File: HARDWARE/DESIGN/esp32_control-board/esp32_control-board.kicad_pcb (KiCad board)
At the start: 2 copper layers, 130 x 105 mm, 140 parts, among them J1 Lock1, J10 ESP32-Prog, J11 RFID-module1, J12 RFID-module2, J15 Lamp1, J16 Lamp2, J17 Lamp3, J18 Lamp4, J19 Lamp5, J2 Lock2, J20 Lamp6, J21 Lamp7, J22 Lamp8, J3 Lock3, J301 ESP32m_Prog, J4 Lock4, J5 Lock5, J6 Lock6, J7 Lock7, J8 Lock8, J9 Power-in, Q1 AO4407C, SW301 Reset, SW302 Boot, U1 ESP32-S3-WROOM-1, U10 PC817, U11 PC817, U12 PC817, U13 PC817, U14 PC817, U15 PC817, U16 PC817, U2 LM63615DQDRRRQ1, U302 USBLC6-2SC6, U4 AMS1117-3.3, U5 PC817, U6 TBD62783A, U7 MCP23008-xSS, U8 MCP23008-xSS, U9 TBD62783A

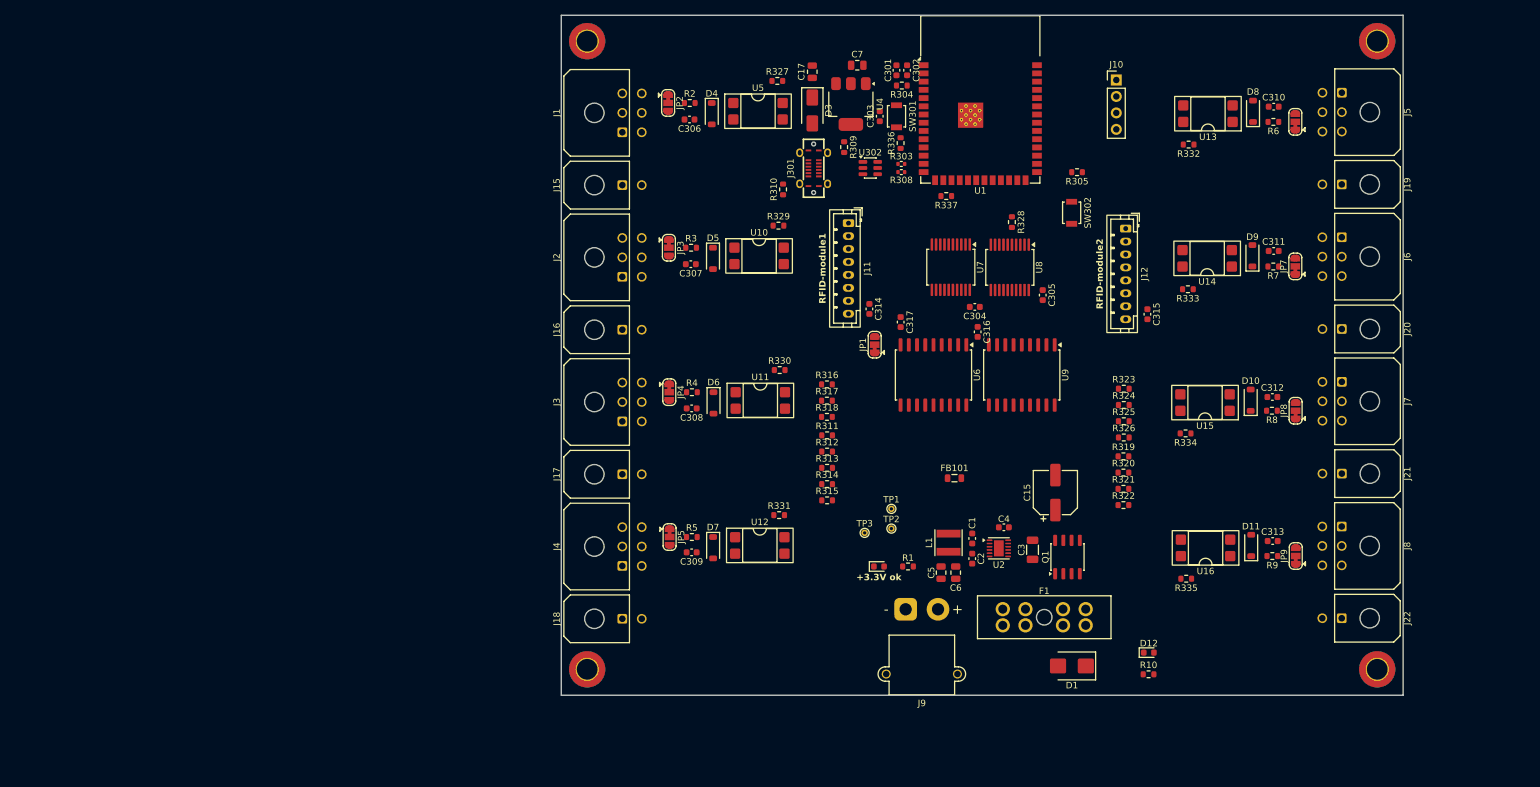
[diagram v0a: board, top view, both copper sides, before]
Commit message: 60710 - schematic and PCB-layout updated
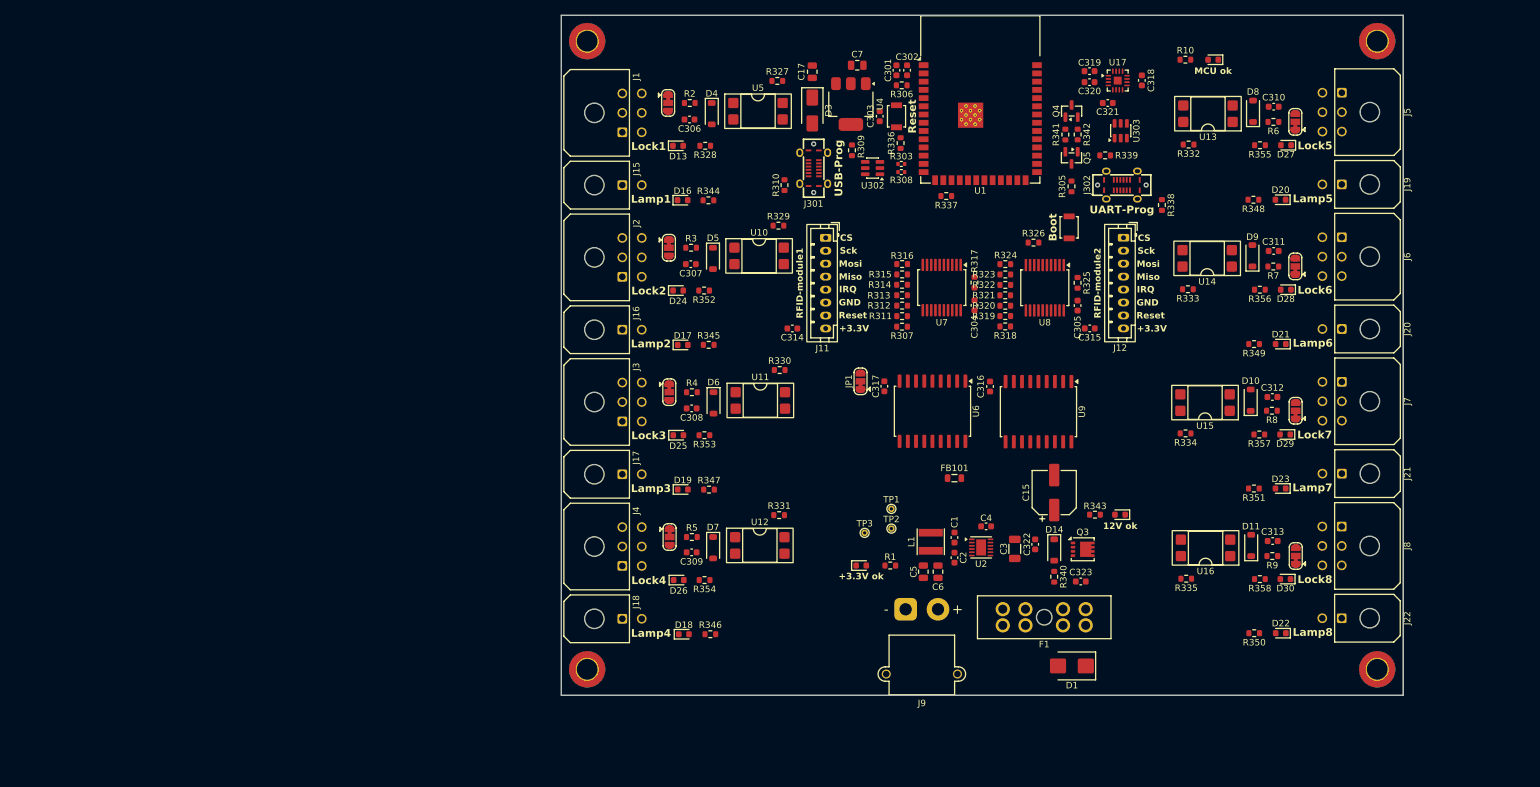
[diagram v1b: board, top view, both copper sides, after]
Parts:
- removed J10: ESP32-Prog, Connector_PinHeader_2.54mm:PinHeader_1x04_P2.54mm_Vertical
- removed Q1: AO4407C, (FOOTPRINTS):SOIC-8_P-MOSFET
- removed R304: 10k, Resistor_SMD:R_0603_1608Metric
- added C318: 100n, Capacitor_SMD:C_0603_1608Metric, F.Cu at (159.9, 60.0)
- added C319: 100n, Capacitor_SMD:C_0603_1608Metric, F.Cu at (151.8, 58.5)
- added C320: 100n, Capacitor_SMD:C_0603_1608Metric, F.Cu at (151.8, 60.2)
- added C321: 100n, Capacitor_SMD:C_0603_1608Metric, F.Cu at (154.6, 63.5)
- added C322: 100n, Capacitor_SMD:C_0603_1608Metric, F.Cu at (143.4, 131.6)
- added C323: 100n, Capacitor_SMD:C_0603_1608Metric, F.Cu at (150.5, 137.3)
- added D13: LOCK on, LED_SMD:LED_0603_1608Metric, F.Cu at (88.3, 70.1)
- added D14: MMSZ5242B, Diode_SMD:D_SOD-123, F.Cu at (146.4, 132.5)
- added D15: MCU ok, LED_SMD:LED_0603_1608Metric, F.Cu at (170.9, 56.8)
- added D16: LAMP on, LED_SMD:LED_0603_1608Metric, F.Cu at (89.0, 78.5)
- added D17: LAMP on, LED_SMD:LED_0603_1608Metric, F.Cu at (89.0, 100.8)
- added D18: LAMP on, LED_SMD:LED_0603_1608Metric, F.Cu at (89.2, 145.5)
- added D19: LAMP on, LED_SMD:LED_0603_1608Metric, F.Cu at (89.0, 123.1)
- added D20: LAMP on, LED_SMD:LED_0603_1608Metric, F.Cu at (181.3, 78.4)
- added D21: LAMP on, LED_SMD:LED_0603_1608Metric, F.Cu at (181.3, 100.7)
- added D22: LAMP on, LED_SMD:LED_0603_1608Metric, F.Cu at (181.4, 145.3)
- added D23: LAMP on, LED_SMD:LED_0603_1608Metric, F.Cu at (181.3, 123.0)
- added D24: LOCK on, LED_SMD:LED_0603_1608Metric, F.Cu at (88.3, 92.4)
- added D25: LOCK on, LED_SMD:LED_0603_1608Metric, F.Cu at (88.3, 114.8)
- added D26: LOCK on, LED_SMD:LED_0603_1608Metric, F.Cu at (88.4, 137.1)
- added D27: LOCK on, LED_SMD:LED_0603_1608Metric, F.Cu at (182.2, 70.0)
- added D28: LOCK on, LED_SMD:LED_0603_1608Metric, F.Cu at (182.1, 92.3)
- added D29: LOCK on, LED_SMD:LED_0603_1608Metric, F.Cu at (182.0, 114.7)
- added D30: LOCK on, LED_SMD:LED_0603_1608Metric, F.Cu at (182.1, 137.0)
- added J302: UART-Prog, (FOOTPRINTS):C3151749_USB_TYPE-C_Vertical, F.Cu at (156.8, 76.1)
- added Q3: DMP3013SFV-7, Package_SON:Diodes_PowerDI3333-8, F.Cu at (150.8, 132.4)
- added Q4: SS8050, Package_TO_SOT_SMD:SOT-23, F.Cu at (149.1, 64.7)
- added Q5: SS8050, Package_TO_SOT_SMD:SOT-23, F.Cu at (149.0, 71.9)
- added R306: 12k, Resistor_SMD:R_0603_1608Metric, F.Cu at (122.8, 60.7)
- added R307: 12k, Resistor_SMD:R_0603_1608Metric, F.Cu at (122.9, 98.0)
- added R338: 5k1, Resistor_SMD:R_0603_1608Metric, F.Cu at (163.0, 79.2)
- added R339: 5k1, Resistor_SMD:R_0603_1608Metric, F.Cu at (154.2, 71.5)
- added R340: 12k, Resistor_SMD:R_0603_1608Metric, F.Cu at (146.4, 136.6)
- added R341: 12k, Resistor_SMD:R_0603_1608Metric, F.Cu at (148.1, 68.3)
- added R342: 12k, Resistor_SMD:R_0603_1608Metric, F.Cu at (150.0, 68.3)
- added R343: 5k1, Resistor_SMD:R_0603_1608Metric, F.Cu at (152.7, 127.0)
- added R344: 5k1, Resistor_SMD:R_0603_1608Metric, F.Cu at (93.0, 78.5)
- added R345: 5k1, Resistor_SMD:R_0603_1608Metric, F.Cu at (93.0, 100.8)
- added R346: 5k1, Resistor_SMD:R_0603_1608Metric, F.Cu at (93.3, 145.5)
- added R347: 5k1, Resistor_SMD:R_0603_1608Metric, F.Cu at (93.1, 123.2)
- added R348: 5k1, Resistor_SMD:R_0603_1608Metric, F.Cu at (177.1, 78.4)
- added R349: 5k1, Resistor_SMD:R_0603_1608Metric, F.Cu at (177.2, 100.7)
- added R350: 5k1, Resistor_SMD:R_0603_1608Metric, F.Cu at (177.3, 145.3)
- added R351: 5k1, Resistor_SMD:R_0603_1608Metric, F.Cu at (177.2, 123.0)
- added R352: 5k1, Resistor_SMD:R_0603_1608Metric, F.Cu at (92.3, 92.4)
- added R353: 5k1, Resistor_SMD:R_0603_1608Metric, F.Cu at (92.4, 114.8)
- added R354: 5k1, Resistor_SMD:R_0603_1608Metric, F.Cu at (92.4, 137.1)
- added R355: 5k1, Resistor_SMD:R_0603_1608Metric, F.Cu at (178.1, 70.0)
- added R356: 5k1, Resistor_SMD:R_0603_1608Metric, F.Cu at (178.1, 92.3)
- added R357: 5k1, Resistor_SMD:R_0603_1608Metric, F.Cu at (178.0, 114.7)
- added R358: 5k1, Resistor_SMD:R_0603_1608Metric, F.Cu at (178.1, 137.0)
- added U17: CH343P, Package_DFN_QFN:TQFN-16-1EP_3x3mm_P0.5mm_EP1.23x1.23mm, F.Cu at (156.2, 60.0)
- added U303: USBLC6-2SC6, Package_TO_SOT_SMD:SOT-23-6, F.Cu at (156.6, 67.8)
- J301: value ESP32m_Prog -> USB-Prog
- R305, R311, R312, R313, R314, R315, R316, R317, R318, R319, R320, R321, R322, R323, R324, R325, R326: value 10k -> 12k
- R328: value 10k -> 5k1
- moved R10 95.1 mm to (166.6, 56.8)
- moved R328 48.8 mm to (92.5, 70.1), turned to 0 degrees
- moved R322 38.6 mm to (138.8, 91.5), turned to 180 degrees
- moved R315 36.8 mm to (122.9, 89.9), turned to 180 degrees
- moved R321 35.0 mm to (138.8, 93.2), turned to 180 degrees
- moved R326 33.2 mm to (143.2, 85.0)
- moved R314 32.9 mm to (122.9, 91.5), turned to 180 degrees
- moved R320 31.6 mm to (138.8, 94.8), turned to 180 degrees
- moved R318 30.9 mm to (138.8, 98.0), turned to 180 degrees
- moved R317 29.2 mm to (134.1, 91.2), turned to -90 degrees
- moved R313 29.1 mm to (122.9, 93.1), turned to 180 degrees
- moved R324 28.4 mm to (138.8, 88.3), turned to 180 degrees
- moved R319 28.3 mm to (138.8, 96.4), turned to 180 degrees
- moved R323 25.4 mm to (138.8, 89.9), turned to 180 degrees
- moved R312 25.3 mm to (122.9, 94.8), turned to 180 degrees
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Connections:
- C317 pad 1: GND -> Net-(JP1-C)
- C317 pad 2: Net-(JP1-C) -> GND
- J301 pad A6: espM_USB_dp -> espU_USB_dp
- J301 pad A7: espM_USB_dm -> espU_USB_dm
- J301 pad B6: espM_USB_dp -> espU_USB_dp
- J301 pad B7: espM_USB_dm -> espU_USB_dm
- R10 pad 1: SWITCH1-COM -> esp_LED
- R10 pad 2: Net-(D12-A) -> Net-(D15-A)
- R303 pad 1: espM_USB_d- -> espU_USB_d-
- R308 pad 1: espM_USB_d+ -> espU_USB_d+
- R311 pad 1: Net-(U6-I1) -> Net-(U6-I7)
- R312 pad 1: Net-(U6-I2) -> Net-(U6-I6)
- R313 pad 1: Net-(U6-I3) -> Net-(U6-I5)
- R315 pad 1: Net-(U6-I5) -> Net-(U6-I3)
- R316 pad 1: Net-(U6-I6) -> Net-(U6-I2)
- R317 pad 1: Net-(U6-I7) -> Net-(U6-I1)
- R318 pad 1: Net-(U6-I8) -> Net-(U8-GP0)
- R319 pad 1: Net-(U8-GP0) -> Net-(U8-GP1)
- R320 pad 1: Net-(U8-GP1) -> Net-(U8-GP2)
- R321 pad 1: Net-(U8-GP2) -> Net-(U8-GP3)
- R322 pad 1: Net-(U8-GP3) -> Net-(U8-GP4)
- R323 pad 1: Net-(U8-GP4) -> Net-(U8-GP5)
- R324 pad 1: Net-(U8-GP5) -> Net-(U8-GP6)
- R325 pad 1: Net-(U8-GP6) -> Net-(U8-GP7)
- R326 pad 1: Net-(U8-GP7) -> +3V3
- R326 pad 2: GND -> Net-(U8-A0)
- R328 pad 1: +3V3 -> Net-(D13-A)
- R328 pad 2: Net-(U8-A0) -> LOCK1_ctrl
- U1 pad 36: esp_Rx -> esp_RXD
- U1 pad 37: esp_Tx -> esp_TXD
- U1 pad 39: unconnected-(U1-IO1-Pad39) -> esp_LED
- U302 pad 1: espM_USB_dm -> espU_USB_d+
- U302 pad 3: espM_USB_dp -> espU_USB_d-
- U302 pad 4: espM_USB_d+ -> espU_USB_dm
- U302 pad 6: espM_USB_d- -> espU_USB_dp
- U6 pad 11: LOCK8_ctrl -> LOCK1_ctrl
- U6 pad 12: LOCK7_ctrl -> LOCK2_ctrl
- U6 pad 13: LOCK6_ctrl -> LOCK3_ctrl
- U6 pad 14: LOCK5_ctrl -> LOCK4_ctrl
- U6 pad 15: LOCK4_ctrl -> LOCK5_ctrl
- U6 pad 16: LOCK3_ctrl -> LOCK6_ctrl
- U6 pad 17: LOCK2_ctrl -> LOCK7_ctrl
- U6 pad 18: LOCK1_ctrl -> LOCK8_ctrl
- U7 pad 12: Net-(U6-I1) -> Net-(U6-I8)
- U7 pad 13: Net-(U6-I2) -> Net-(U6-I7)
- U7 pad 14: Net-(U6-I3) -> Net-(U6-I6)
- U7 pad 15: Net-(U6-I4) -> Net-(U6-I5)
- U7 pad 16: Net-(U6-I5) -> Net-(U6-I4)
- U7 pad 17: Net-(U6-I6) -> Net-(U6-I3)
- U7 pad 18: Net-(U6-I7) -> Net-(U6-I2)
- U7 pad 19: Net-(U6-I8) -> Net-(U6-I1)
- U9 pad 1: Net-(U8-GP0) -> Net-(U8-GP7)
- U9 pad 11: LAMP8 -> LAMP1
- U9 pad 12: LAMP7 -> LAMP2
- U9 pad 13: LAMP6 -> LAMP3
- U9 pad 14: LAMP5 -> LAMP4
- U9 pad 15: LAMP4 -> LAMP5
- U9 pad 16: LAMP3 -> LAMP6
- U9 pad 17: LAMP2 -> LAMP7
- U9 pad 18: LAMP1 -> LAMP8
- U9 pad 2: Net-(U8-GP1) -> Net-(U8-GP6)
- U9 pad 3: Net-(U8-GP2) -> Net-(U8-GP5)
- U9 pad 4: Net-(U8-GP3) -> Net-(U8-GP4)
- U9 pad 5: Net-(U8-GP4) -> Net-(U8-GP3)
- U9 pad 6: Net-(U8-GP5) -> Net-(U8-GP2)
- U9 pad 7: Net-(U8-GP6) -> Net-(U8-GP1)
- U9 pad 8: Net-(U8-GP7) -> Net-(U8-GP0)
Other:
- board text added: "+3.3V"
- board text added: "CS"
- board text added: "GND"
- board text added: "IRQ"
- board text added: "Miso"
- board text added: "Mosi"
- board text added: "Reset"
- board text added: "Sck"

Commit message: 60714 - one of two I2C-mux ICs was removed, PCB-layout finished, start tracing
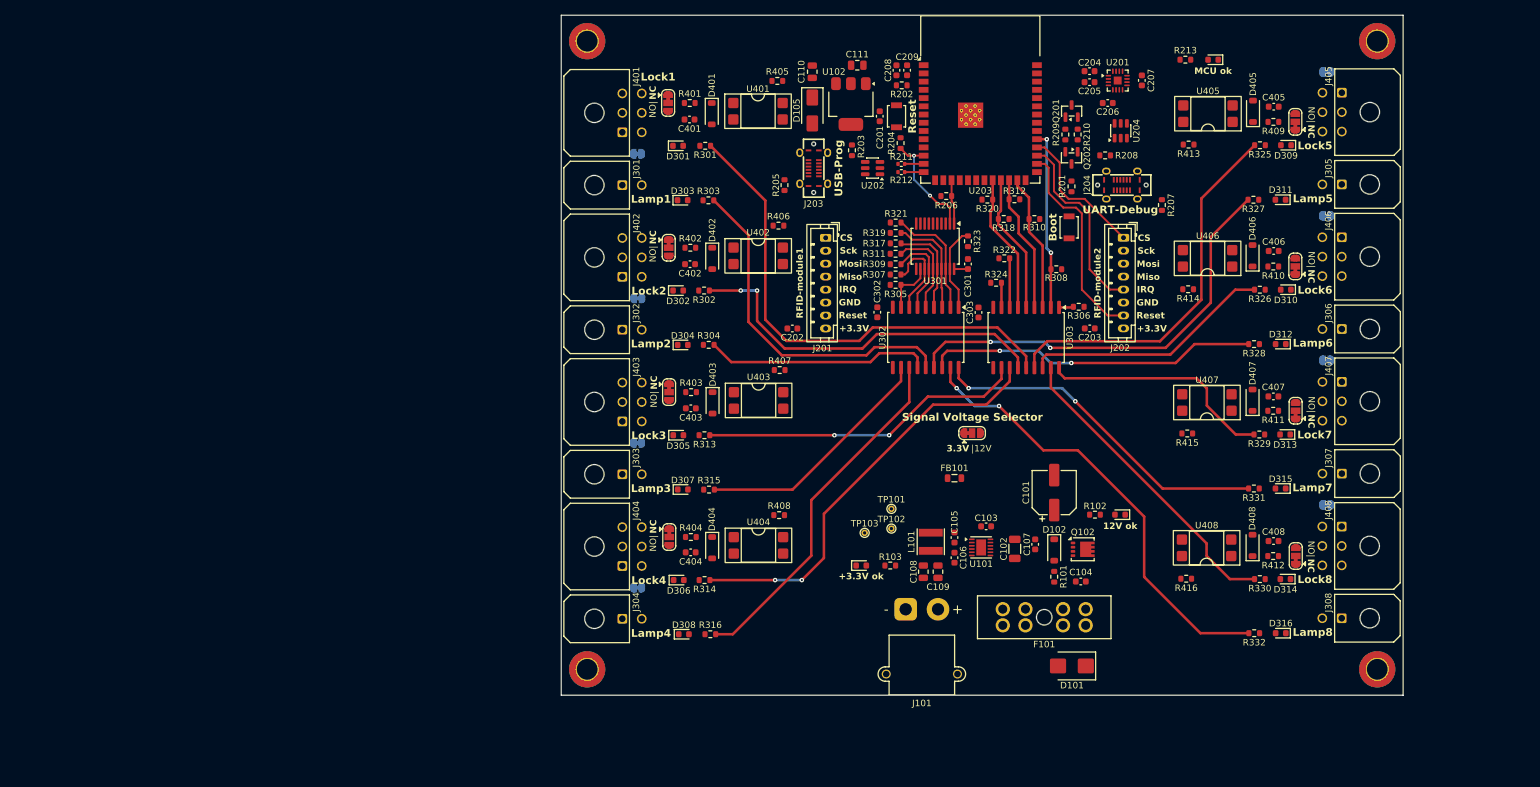
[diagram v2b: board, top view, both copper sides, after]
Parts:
- removed C304: 100n, Capacitor_SMD:C_0603_1608Metric
- removed the R326 at (143.2, 85.0)
- removed U6: TBD62783A, Package_SO:SOIC-18W_7.5x11.6mm_P1.27mm
- removed U7: MCP23008-xSS, Package_SO:SSOP-20_5.3x7.2mm_P0.65mm
- added JP409: 12V-to-COM, Jumper:SolderJumper-2_P1.3mm_Bridged_RoundedPad1.0x1.5mm, B.Cu at (82.0, 71.3)
- added JP410: 12V-to-COM, Jumper:SolderJumper-2_P1.3mm_Bridged_RoundedPad1.0x1.5mm, B.Cu at (82.1, 93.6)
- added JP411: 12V-to-COM, Jumper:SolderJumper-2_P1.3mm_Bridged_RoundedPad1.0x1.5mm, B.Cu at (82.0, 115.9)
- added JP412: 12V-to-COM, Jumper:SolderJumper-2_P1.3mm_Bridged_RoundedPad1.0x1.5mm, B.Cu at (82.0, 138.3)
- added JP413: 12V-to-COM, Jumper:SolderJumper-2_P1.3mm_Bridged_RoundedPad1.0x1.5mm, B.Cu at (188.4, 58.7)
- added JP414: 12V-to-COM, Jumper:SolderJumper-2_P1.3mm_Bridged_RoundedPad1.0x1.5mm, B.Cu at (188.4, 80.9)
- added JP415: 12V-to-COM, Jumper:SolderJumper-2_P1.3mm_Bridged_RoundedPad1.0x1.5mm, B.Cu at (188.4, 103.2)
- added JP416: 12V-to-COM, Jumper:SolderJumper-2_P1.3mm_Bridged_RoundedPad1.0x1.5mm, B.Cu at (188.4, 125.5)
- added U303: TBD62783A, Package_SO:SOIC-18W_7.5x11.6mm_P1.27mm, F.Cu at (142.0, 99.7)
- J204: renamed from J302; value UART-Prog -> UART-Debug
- moved R306 27.5 mm to (150.2, 94.9), turned to 0 degrees
- moved R308 24.9 mm to (146.7, 89.1), turned to 0 degrees
- moved R310 24.4 mm to (143.3, 81.4), turned to 0 degrees
- moved R312 22.8 mm to (140.2, 78.3), turned to 0 degrees
- moved C302 20.8 mm to (119.0, 95.8)
- moved U302 20.8 mm to (126.5, 99.7)
- moved JP301 19.0 mm to (133.7, 114.4), turned to 0 degrees
- moved R318 18.7 mm to (138.6, 81.4), turned to 0 degrees
- moved C303 18.5 mm to (134.7, 95.8)
- moved R307 18.1 mm to (121.9, 89.9)
- moved R305 18.1 mm to (121.9, 91.5)
- moved R311 18.1 mm to (121.9, 86.7)
- moved R321 18.1 mm to (121.9, 81.9)
- moved R309 18.1 mm to (121.9, 88.4)
- moved R317 18.1 mm to (121.9, 85.1)
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- renumbered C15 to C101, C3 to C102, C4 to C103, C323 to C104, C1 to C105, C2 to C106, C322 to C107, C5 to C108, C6 to C109, C17 to C110, C7 to C111, C303 to C201, C314 to C202, C315 to C203, C319 to C204, C320 to C205, C321 to C206, C318 to C207, C301 to C208, C302 to C209, C305 to C301, C316 to C302, C317 to C303, C306 to C401, C307 to C402, C308 to C403, C309 to C404, C310 to C405, C311 to C406, C312 to C407, C313 to C408, D1 to D101, D14 to D102, D12 to D103, D2 to D104, D3 to D105, D15 to D201, D13 to D301, D24 to D302, D16 to D303, D17 to D304, D25 to D305, D26 to D306, D19 to D307, D18 to D308, D27 to D309, D28 to D310, D20 to D311, D21 to D312, D29 to D313, D30 to D314, D23 to D315, D22 to D316, D4 to D401, D5 to D402, D6 to D403, D7 to D404, D8 to D405, D9 to D406, D10 to D407, D11 to D408, F1 to F101, J9 to J101, J11 to J201, J12 to J202, J301 to J203, J15 to J301, J16 to J302, J17 to J303, J18 to J304, J19 to J305, J20 to J306, J21 to J307, J22 to J308, J1 to J401, J2 to J402, J3 to J403, J4 to J404, J5 to J405, J6 to J406, J7 to J407, J8 to J408, JP1 to JP301, JP2 to JP401, JP3 to JP402, JP4 to JP403, JP5 to JP404, JP6 to JP405, JP7 to JP406, JP8 to JP407, JP9 to JP408, L1 to L101, Q3 to Q102, Q4 to Q201, Q5 to Q202, R340 to R101, R343 to R102, R1 to R103, R305 to R201, R306 to R202, R309 to R203, R336 to R204, R310 to R205, R337 to R206, R338 to R207, R339 to R208, R341 to R209, R342 to R210, R303 to R211, R308 to R212, R10 to R213, R328 to R301, R352 to R302, R344 to R303, R345 to R304, R318 to R305, R307 to R306, R319 to R307, R311 to R308, R320 to R309, R312 to R310, R321 to R311, R313 to R312, R353 to R313, R354 to R314, R347 to R315, R346 to R316, R322 to R317, R314 to R318, R323 to R319, R315 to R320, R324 to R321, R316 to R322, R325 to R323, R317 to R324, R355 to R325, R356 to R326, R348 to R327, R349 to R328, R357 to R329, R358 to R330, R351 to R331, R350 to R332, R2 to R401, R3 to R402, R4 to R403, R5 to R404, R327 to R405, R329 to R406, R330 to R407, R331 to R408, R6 to R409, R7 to R410, R8 to R411, R9 to R412, R332 to R413, R333 to R414, R334 to R415, R335 to R416, SW302 to SW201, SW301 to SW202, TP1 to TP101, TP2 to TP102, TP3 to TP103, U2 to U101, U4 to U102, U17 to U201, U302 to U202, U1 to U203, U303 to U204, U8 to U301, U9 to U302, U5 to U401, U10 to U402, U11 to U403, U12 to U404, U13 to U405, U14 to U406, U15 to U407, U16 to U408
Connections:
- C101 pad 1: SWITCH1-COM -> +12V
- C102 pad 1: SWITCH1-COM -> +12V
- C103 pad 1: SWITCH1-COM -> +12V
- C107 pad 2: SWITCH1-COM -> +12V
- C302 pad 2: SWITCH1-COM -> +12V
- D102 pad 1: SWITCH1-COM -> +12V
- J401 pad 2: SWITCH1-COM -> +12V
- J402 pad 2: SWITCH1-COM -> +12V
- J402 pad 4: SWITCH1-COM -> SWITCH2-COM
- J403 pad 2: SWITCH1-COM -> +12V
- J403 pad 4: SWITCH1-COM -> SWITCH3-COM
- J404 pad 2: SWITCH1-COM -> +12V
- J404 pad 4: SWITCH1-COM -> SWITCH4-COM
- J405 pad 2: SWITCH1-COM -> +12V
- J405 pad 4: SWITCH1-COM -> SWITCH5-COM
- J406 pad 2: SWITCH1-COM -> +12V
- J406 pad 4: SWITCH1-COM -> SWITCH6-COM
- J407 pad 2: SWITCH1-COM -> +12V
- J407 pad 4: SWITCH1-COM -> SWITCH7-COM
- J408 pad 2: SWITCH1-COM -> +12V
- J408 pad 4: SWITCH1-COM -> SWITCH8-COM
- JP301 pad 3: SWITCH1-COM -> +12V
- Q102 pad 1: SWITCH1-COM -> +12V
- Q102 pad 2: SWITCH1-COM -> +12V
- Q102 pad 3: SWITCH1-COM -> +12V
- R102 pad 2: SWITCH1-COM -> +12V
- R306 pad 1: Net-(U6-I8) -> LOCK1_do
- R308 pad 1: Net-(U6-I7) -> LOCK2_do
- R310 pad 1: Net-(U6-I6) -> LOCK3_do
- R312 pad 1: Net-(U6-I5) -> LOCK4_do
- R318 pad 1: Net-(U6-I4) -> LOCK5_do
- R320 pad 1: Net-(U6-I3) -> LOCK6_do
- R322 pad 1: Net-(U6-I2) -> LOCK7_do
- R324 pad 1: Net-(U6-I1) -> LOCK8_do
- U101 pad 10: SWITCH1-COM -> +12V
- U101 pad 12: SWITCH1-COM -> +12V
- U203 pad 10: GPIO17 -> LOCK7_do
- U203 pad 11: GPIO18 -> LOCK8_do
- U203 pad 22: unconnected-(U1-IO14-Pad22) -> LOCK6_do
- U203 pad 23: GPIO21 -> LOCK5_do
- U203 pad 24: GPIO47 -> LOCK4_do
- U203 pad 25: GPIO48 -> LOCK3_do
- U203 pad 28: unconnected-(U1-IO35-Pad28) -> RFID2_reset
- U203 pad 29: unconnected-(U1-IO36-Pad29) -> RFID2_irq
- U203 pad 30: unconnected-(U1-IO37-Pad30) -> SPI_cs2
- U203 pad 31: GPIO38 -> LOCK2_do
- U203 pad 32: GPIO39 -> LOCK1_do
- U203 pad 33: GPIO40 -> LOCK8_signal
- U203 pad 34: GPIO41 -> LOCK7_signal
- U203 pad 35: GPIO42 -> LOCK6_signal
- U203 pad 38: unconnected-(U1-IO2-Pad38) -> LOCK5_signal
- U203 pad 4: unconnected-(U1-IO4-Pad4) -> LOCK1_signal
- U203 pad 5: unconnected-(U1-IO5-Pad5) -> LOCK2_signal
- U203 pad 6: unconnected-(U1-IO6-Pad6) -> LOCK3_signal
- U203 pad 7: unconnected-(U1-IO7-Pad7) -> LOCK4_signal
- U203 pad 8: unconnected-(U1-IO15-Pad8) -> RFID1_irq
- U203 pad 9: unconnected-(U1-IO16-Pad9) -> RFID1_reset
- U301 pad 5: Net-(U8-A0) -> GND
- U302 pad 11: LAMP1 -> LAMP3
- U302 pad 12: LAMP2 -> LAMP4
- U302 pad 13: LAMP3 -> LAMP2
- U302 pad 14: LAMP4 -> LAMP1
- U302 pad 17: LAMP7 -> LAMP8
- U302 pad 18: LAMP8 -> LAMP7
- U302 pad 9: SWITCH1-COM -> +12V
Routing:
- net LOCK1_ctrl: track 0.00 -> 76.5 mm
- net LAMP8: track 0.00 -> 69.8 mm, vias 0 -> 2
- net LAMP5: track 0.00 -> 67.2 mm, vias 0 -> 2
- net LOCK4_ctrl: track 0.00 -> 65.1 mm, vias 0 -> 2
- net LOCK5_ctrl: track 0.00 -> 58.6 mm
- net LOCK2_ctrl: track 0.00 -> 58.1 mm, vias 0 -> 2
- net LAMP4: track 0.00 -> 55.1 mm
- net LAMP7: track 0.00 -> 53.5 mm, vias 0 -> 2
- net LAMP1: track 0.00 -> 53.4 mm
- net LAMP6: track 0.00 -> 51.5 mm, vias 0 -> 2
- net LOCK3_ctrl: track 0.00 -> 50.4 mm, vias 0 -> 2
- net LOCK8_ctrl: track 0.00 -> 47.9 mm
- net LOCK6_ctrl: track 0.00 -> 38.6 mm
- net LAMP3: track 0.00 -> 37.9 mm
- net LOCK7_ctrl: track 0.00 -> 36.4 mm
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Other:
- board text added: "3.3V"
- board text added: "NC"
- board text added: "NO|"
- board text added: "|12V"

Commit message: 60714 - traced 20%
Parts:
- moved C301 1.99 mm to (131.1, 88.4)
- moved R309 1.99 mm to (119.9, 88.5)
- moved R323 1.99 mm to (131.1, 84.9)
- moved R307 1.99 mm to (119.9, 90.0)
- moved R305 1.99 mm to (119.9, 91.6)
- moved R311 1.99 mm to (119.9, 86.8)
- moved R317 1.99 mm to (119.9, 85.2)
- moved R319 1.99 mm to (119.9, 83.6)
- moved R321 1.99 mm to (119.9, 82.0)
- moved U301 1.99 mm to (126.0, 85.7)
- moved R322 0.88 mm to (138.7, 88.3)
- moved U102 0.67 mm to (114.8, 64.3)
- moved C111 0.67 mm to (115.8, 58.3)
- moved R407 0.28 mm to (103.7, 104.7)
- moved R408 0.21 mm to (103.7, 127.1)
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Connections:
- U202 pad 5: +5V_usb -> Vusb
- U203 pad 8: RFID1_irq -> RFID1_reset
- U203 pad 9: RFID1_reset -> RFID1_irq
- U204 pad 5: +5V_usb -> Vusb
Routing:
- net LOCK4_signal: track 0.00 -> 77.3 mm, vias 0 -> 2
- net LOCK3_signal: track 0.00 -> 57.1 mm, vias 0 -> 2
- net RFID1_reset: track 0.00 -> 41.6 mm, vias 0 -> 1
- net Vusb: track 0.00 -> 38.9 mm, vias 0 -> 4
- net LOCK2_signal: track 0.00 -> 35.9 mm, vias 0 -> 2
- net RFID1_irq: track 0.00 -> 35.0 mm, vias 0 -> 1
- net +3V3: track 2.15 -> 36.3 mm, vias 0 -> 1
- net LOCK8_do: track 3.81 -> 32.6 mm, vias 0 -> 2
- net LOCK1_signal: track 0.00 -> 26.1 mm, vias 0 -> 2
- net LOCK7_do: track 7.59 -> 33.6 mm, vias 0 -> 2
- net GND: track 0.00 -> 25.8 mm
- net espU_USB_dm: track 0.00 -> 14.9 mm, vias 0 -> 3
- net esp_Reset: track 0.00 -> 9.52 mm
- net espU_USB_dp: track 0.00 -> 9.45 mm
- net Net-(D105-K): track 0.00 -> 7.14 mm
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
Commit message: 60714 - traced 25%
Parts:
- moved R416 0.34 mm to (167.1, 136.9)
- moved R415 0.20 mm to (167.1, 114.4)
- moved U408 0.18 mm to (170.1, 132.2)
- moved U407 0.14 mm to (170.1, 109.7)
- moved R414 0.08 mm to (167.1, 92.2)
- moved U403 0.06 mm to (100.7, 109.4)
- moved R413 0.05 mm to (167.1, 69.8)
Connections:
- U203 pad 1: GND -> GND_MCU
- U203 pad 40: GND -> GND_MCU
- U203 pad 41: GND -> GND_MCU
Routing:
- net GND_MCU: track 0.00 -> 153.0 mm, vias 0 -> 8
- net GND: track 25.8 -> 139.5 mm
- net +12V: track 0.00 -> 38.3 mm
- net LOCK4_ctrl: track 65.1 -> 90.5 mm
- net LOCK2_ctrl: track 58.1 -> 83.5 mm
- net LOCK3_ctrl: track 50.4 -> 75.8 mm
- net LOCK1_ctrl: track 76.5 -> 101.8 mm
- net LAMP4: track 55.1 -> 72.5 mm
- net LAMP3: track 37.9 -> 55.0 mm
- net LAMP2: track 34.9 -> 52.0 mm
- net LAMP1: track 53.4 -> 70.4 mm
- net Net-(D401-K): track 0.00 -> 5.90 mm
- net Net-(D402-K): track 0.00 -> 5.85 mm
- net Net-(D404-K): track 0.00 -> 5.81 mm
- net Net-(D403-K): track 0.00 -> 5.76 mm
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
